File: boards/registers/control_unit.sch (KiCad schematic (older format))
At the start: 0 parts

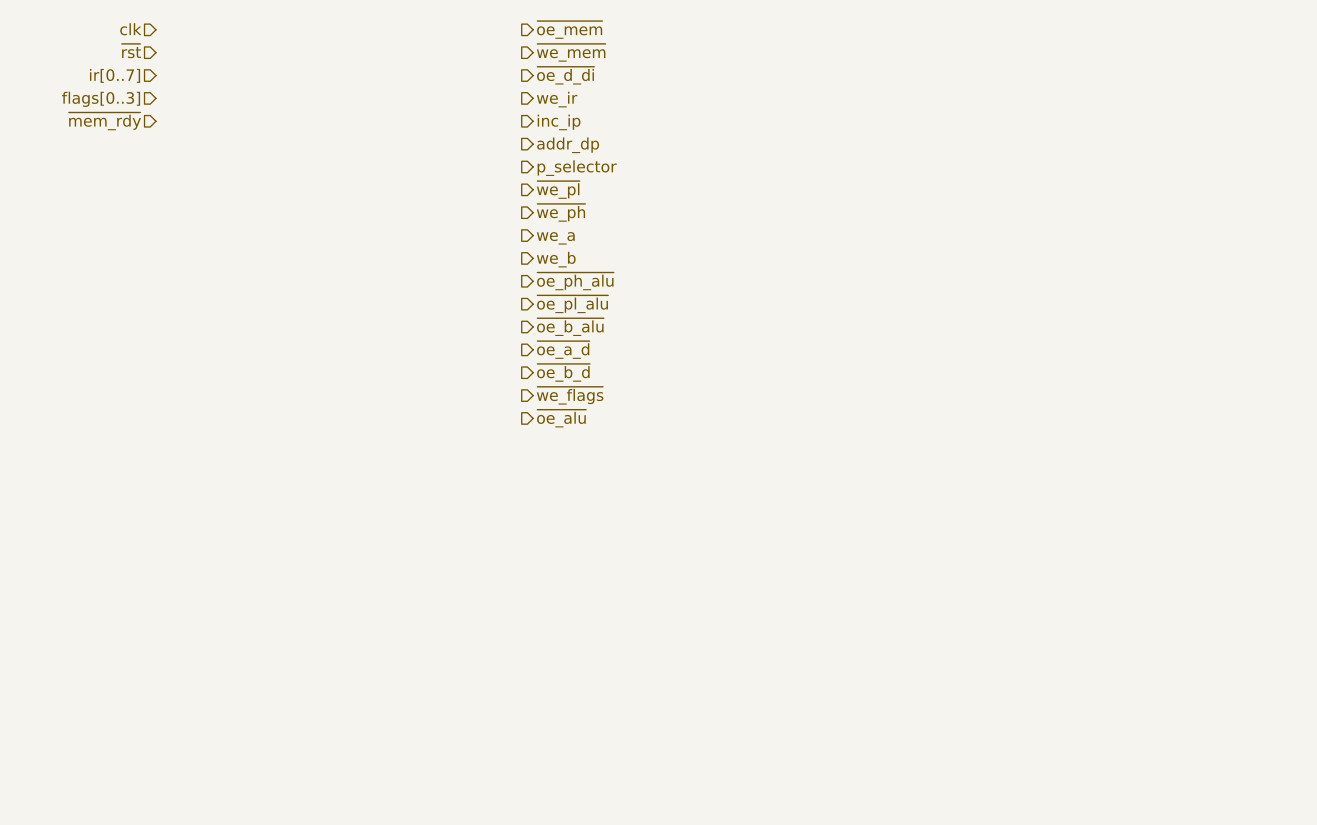
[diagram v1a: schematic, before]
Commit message: IO, ALU, and CU connectors
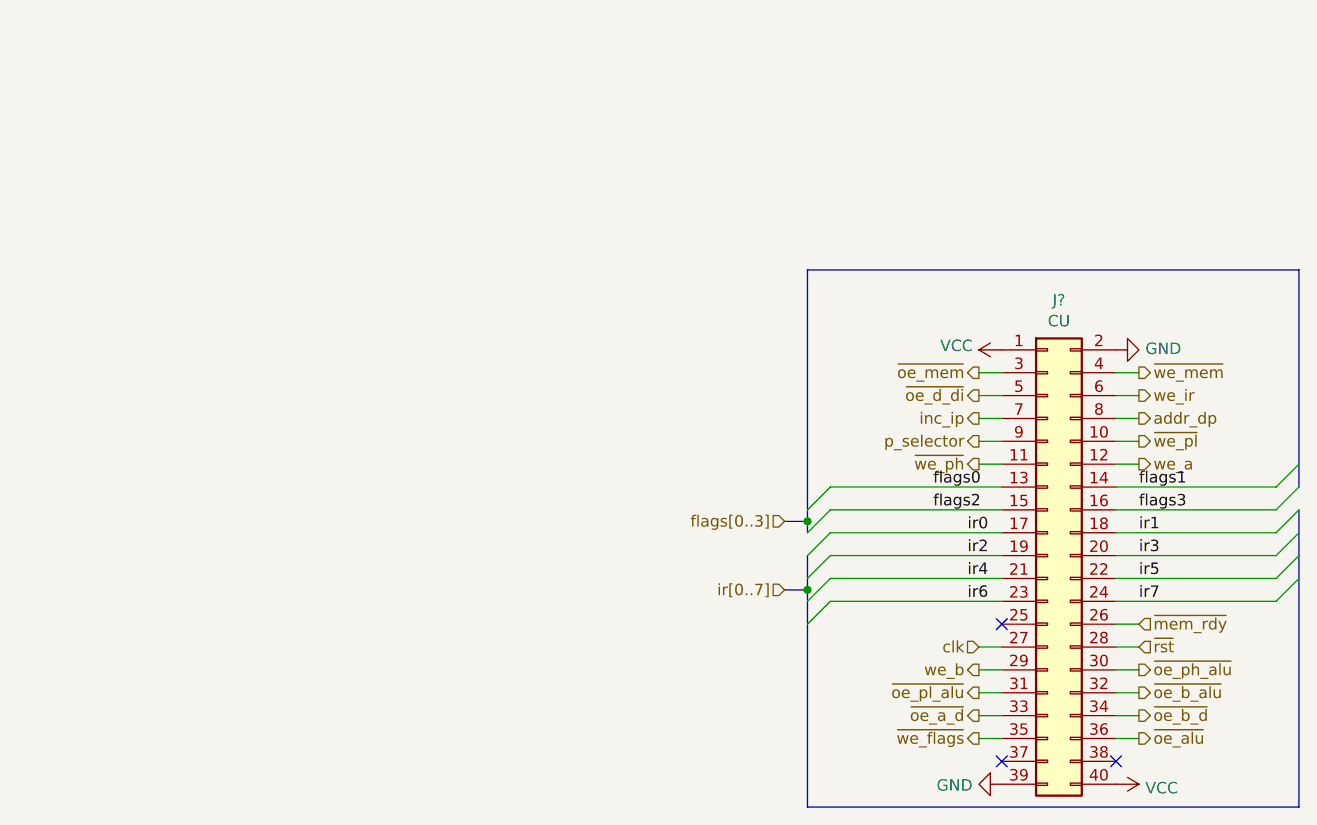
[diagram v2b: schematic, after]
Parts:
- added J?: CU, symbol Connector_Generic:Conn_02x20_Odd_Even
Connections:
- net addr_dp: now also J?.8 (Pin_8)
- net clk: now also J?.27 (Pin_27)
- net inc_ip: now also J?.7 (Pin_7)
- net p_selector: now also J?.9 (Pin_9)
- net we_a: now also J?.12 (Pin_12)
- net we_b: now also J?.29 (Pin_29)
- net we_ir: now also J?.6 (Pin_6)
- net ~mem_rdy: now also J?.26 (Pin_26)
- net ~oe_a_d: now also J?.33 (Pin_33)
- net ~oe_alu: now also J?.36 (Pin_36)
- net ~oe_b_alu: now also J?.32 (Pin_32)
- net ~oe_b_d: now also J?.34 (Pin_34)
- net ~oe_d_di: now also J?.5 (Pin_5)
- net ~oe_mem: now also J?.3 (Pin_3)
- net ~oe_ph_alu: now also J?.30 (Pin_30)
- net ~oe_pl_alu: now also J?.31 (Pin_31)
- net ~rst: now also J?.28 (Pin_28)
- net ~we_flags: now also J?.35 (Pin_35)
- net ~we_mem: now also J?.4 (Pin_4)
- net ~we_ph: now also J?.11 (Pin_11)
- net ~we_pl: now also J?.10 (Pin_10)
- new net GND: J?.2 (Pin_2), J?.39 (Pin_39)
- new net VCC: J?.1 (Pin_1), J?.40 (Pin_40)
- new net flags0: J?.13 (Pin_13)
- new net flags1: J?.14 (Pin_14)
- new net flags2: J?.15 (Pin_15)
- new net flags3: J?.16 (Pin_16)
- new net ir0: J?.17 (Pin_17)
- new net ir1: J?.18 (Pin_18)
- new net ir2: J?.19 (Pin_19)
- new net ir3: J?.20 (Pin_20)
- new net ir4: J?.21 (Pin_21)
- new net ir5: J?.22 (Pin_22)
- new net ir6: J?.23 (Pin_23)
- new net ir7: J?.24 (Pin_24)
- no-connect marks 0 -> 3

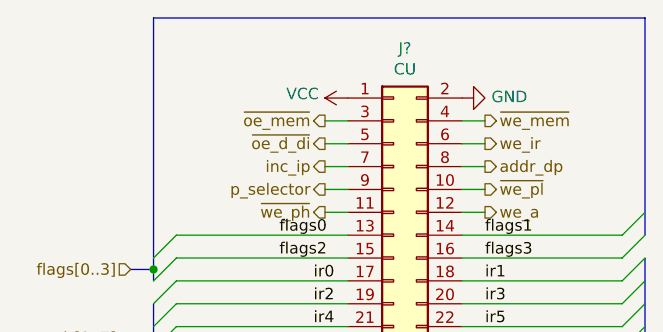
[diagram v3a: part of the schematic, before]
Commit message: Annotated schematics, assigned footprints
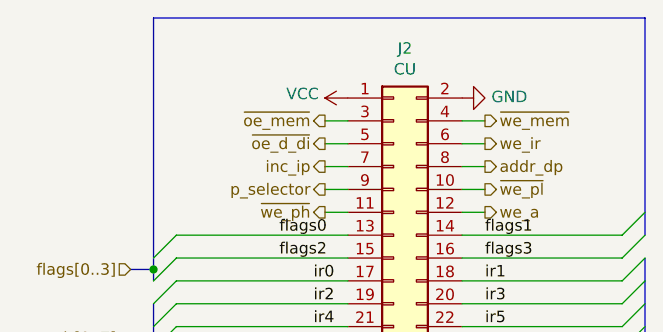
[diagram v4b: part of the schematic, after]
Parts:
- J2: renamed from J?; footprint (none) -> Connector_PinSocket_2.54mm:PinSocket_2x20_P2.54mm_Horizontal
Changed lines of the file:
@@
 ~oe_b_alu
 $Comp
-L Connector_Generic:Conn_02x20_Odd_Even J?
+L Connector_Generic:Conn_02x20_Odd_Even J2
 U 1 1 5EDA71CD
 P 5850 3700
-F 0 "J?" H 5900 4817 50  0000 C CNN
+F 0 "J2" H 5900 4817 50  0000 C CNN
 F 1 "CU" H 5900 4726 50  0000 C CNN
-F 2 "" H 5850 3700 50  0001 C CNN
+F 2 "Connector_PinSocket_2.54mm:PinSocket_2x20_P2.54mm_Horizontal" H 5850 3700 50  0001 C CNN
 F 3 "~" H 5850 3700 50  0001 C CNN
 	1    5850 3700
@@
 $EndComp
 $Comp
-L power:VCC #PWR?
+L power:VCC #PWR0190
 U 1 1 5EDAB67E
 P 5650 2800
-F 0 "#PWR?" H 5650 2650 50  0001 C CNN
+F 0 "#PWR0190" H 5650 2650 50  0001 C CNN
 F 1 "VCC" V 5668 2927 50  0000 L CNN
 F 2 "" H 5650 2800 50  0001 C CNN
@@
 $EndComp
 $Comp
-L power:VCC #PWR?
+L power:VCC #PWR0193
 U 1 1 5EDABE71
 P 6150 4700
-F 0 "#PWR?" H 6150 4550 50  0001 C CNN
+F 0 "#PWR0193" H 6150 4550 50  0001 C CNN
 F 1 "VCC" V 6167 4828 50  0000 L CNN
 F 2 "" H 6150 4700 50  0001 C CNN
@@
 $EndComp
 $Comp
-L power:GND #PWR?
+L power:GND #PWR0191
 U 1 1 5EDAC68A
 P 5650 4700
-F 0 "#PWR?" H 5650 4450 50  0001 C CNN
+F 0 "#PWR0191" H 5650 4450 50  0001 C CNN
 F 1 "GND" V 5655 4572 50  0000 R CNN
 F 2 "" H 5650 4700 50  0001 C CNN
@@
 $EndComp
 $Comp
-L power:GND #PWR?
+L power:GND #PWR0192
 U 1 1 5EDACBD5
 P 6150 2800
-F 0 "#PWR?" H 6150 2550 50  0001 C CNN
+F 0 "#PWR0192" H 6150 2550 50  0001 C CNN
 F 1 "GND" V 6155 2672 50  0000 R CNN
 F 2 "" H 6150 2800 50  0001 C CNN

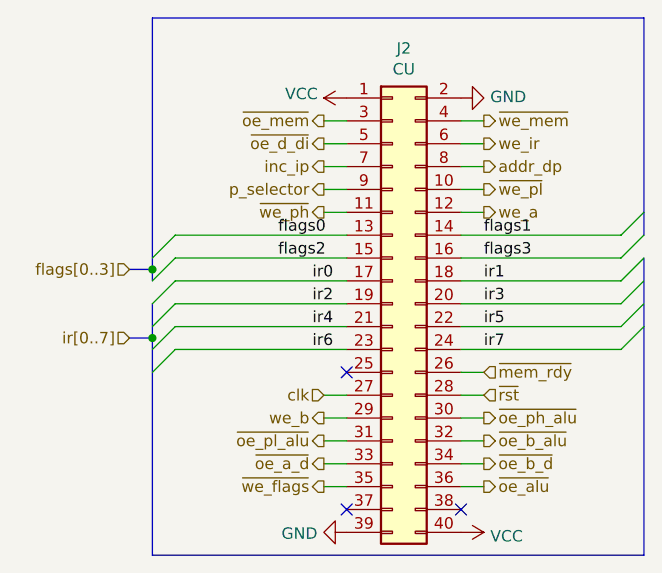
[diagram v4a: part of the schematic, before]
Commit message: CPU registers board
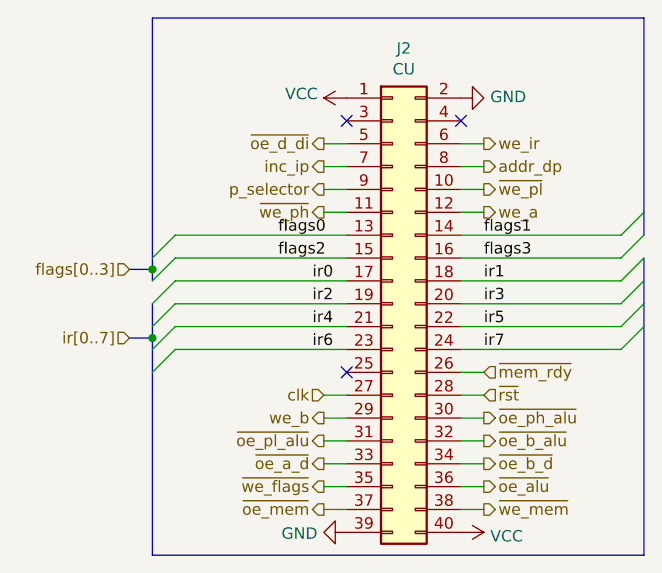
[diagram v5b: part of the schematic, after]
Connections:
- net ~oe_mem: now also J2.37 (Pin_37); no longer J2.3 (Pin_3)
- net ~we_mem: now also J2.38 (Pin_38); no longer J2.4 (Pin_4)
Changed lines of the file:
@@
 Text HLabel 6250 4000 2    50   Input ~ 0
 ~mem_rdy
-Text HLabel 6250 2900 2    50   Output ~ 0
+Text HLabel 6250 4600 2    50   Output ~ 0
 ~we_mem
 Text HLabel 5550 3000 0    50   Output ~ 0
@@
 Wire Wire Line
 	5650 4100 5550 4100
-Text HLabel 5550 2900 0    50   Output ~ 0
+Text HLabel 5550 4600 0    50   Output ~ 0
 ~oe_mem
 Wire Wire Line
@@
 	6150 4100 6250 4100
 NoConn ~ 5650 4000
-NoConn ~ 6150 4600
-NoConn ~ 5650 4600
+NoConn ~ 5650 2900
+NoConn ~ 6150 2900
 Wire Wire Line
 	5650 4500 5550 4500
@@
 	6150 3000 6250 3000
 Wire Wire Line
-	6250 2900 6150 2900
-Wire Wire Line
-	5650 2900 5550 2900
+	6250 4600 6150 4600
+Wire Wire Line
+	5650 4600 5550 4600
 Wire Wire Line
 	5550 3000 5650 3000

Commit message: Part names
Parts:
- J2: value CU -> SSW-120-02-G-D-RA
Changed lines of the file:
@@
 P 5850 3700
 F 0 "J2" H 5900 4817 50  0000 C CNN
-F 1 "CU" H 5900 4726 50  0000 C CNN
+F 1 "SSW-120-02-G-D-RA" H 5900 4726 50  0000 C CNN
 F 2 "Connector_PinSocket_2.54mm:PinSocket_2x20_P2.54mm_Horizontal" H 5850 3700 50  0001 C CNN
 F 3 "~" H 5850 3700 50  0001 C CNN

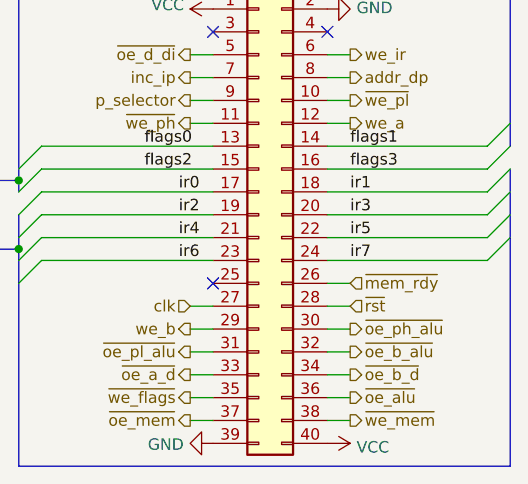
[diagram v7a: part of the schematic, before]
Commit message: Registers: new clock and reset
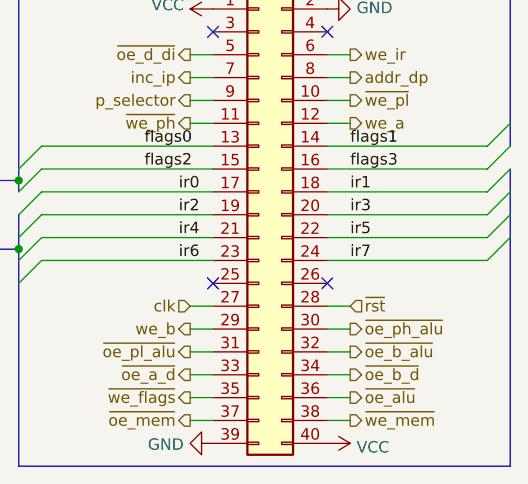
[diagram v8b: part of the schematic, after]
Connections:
- net ~mem_rdy: no longer names the net of J2.26 (Pin_26)
- no-connect marks 3 -> 4
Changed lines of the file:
@@
 Text HLabel 4700 3550 0    50   Input ~ 0
 flags[0..3]
-Text HLabel 6250 4000 2    50   Input ~ 0
-~mem_rdy
 Text HLabel 6250 4600 2    50   Output ~ 0
 ~we_mem
@@
 	4800 3550 4800 3600
 Wire Wire Line
-	6250 4000 6150 4000
-Wire Wire Line
 	6150 4100 6250 4100
 NoConn ~ 5650 4000
@@
 Wire Wire Line
 	5650 3300 5550 3300
+NoConn ~ 6150 4000
 Wire Bus Line
 	4800 3700 4800 3850
